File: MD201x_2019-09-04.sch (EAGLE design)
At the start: 103 parts, among them IC1 78L05F, IC2 LM321MF, J1 8P8C-LED, J10 1744446-4, J2 1744446-4, J3 XH-4-SIDE, J4 MA04-2, J5 MA05-2, J6 MA02-2, Q1 N-MOSFET-, Q2 N-MOSFET-, Q3 N-MOSFET-, Q4 N-MOSFET-, Q5 BSS123, U1 STM32F103C8, U10 XC6206, U2 NCV7351D1E, U3 SI8621AB-B-IS, U4 TLP184, U5 NCP5106D, U6 NCP5106D, U7 NCS199, U8 7815DT, U9 7805DT, X1 CSTCE8M00G55

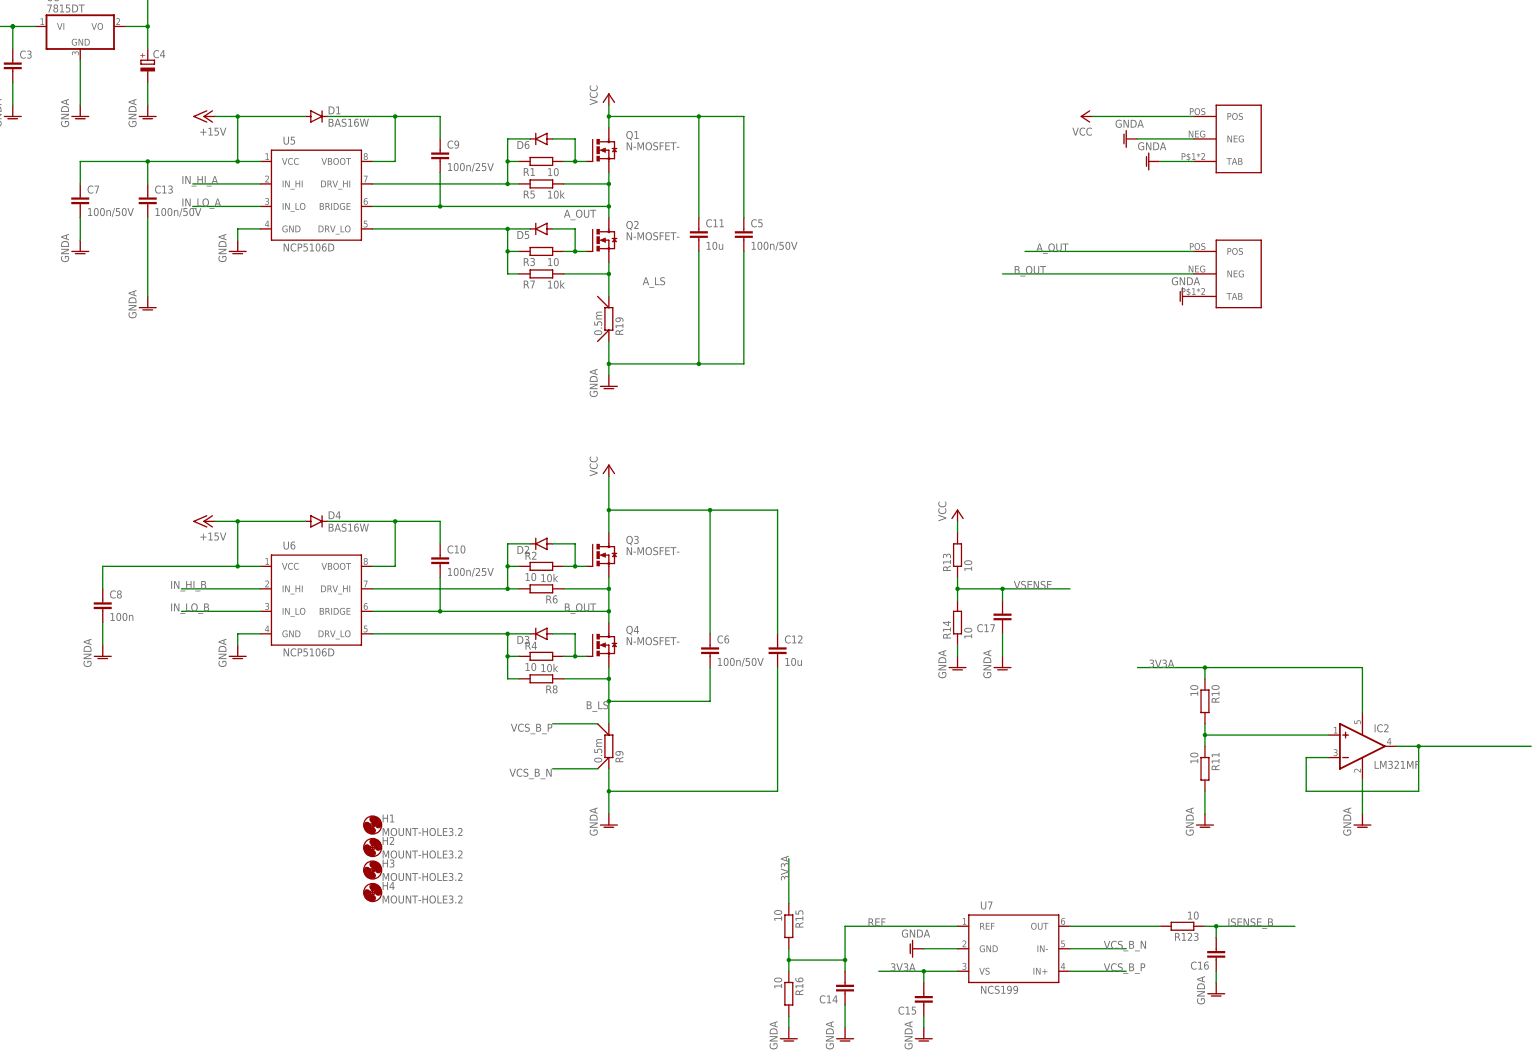
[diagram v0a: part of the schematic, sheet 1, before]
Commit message: エンコーダとand回路周りの修正
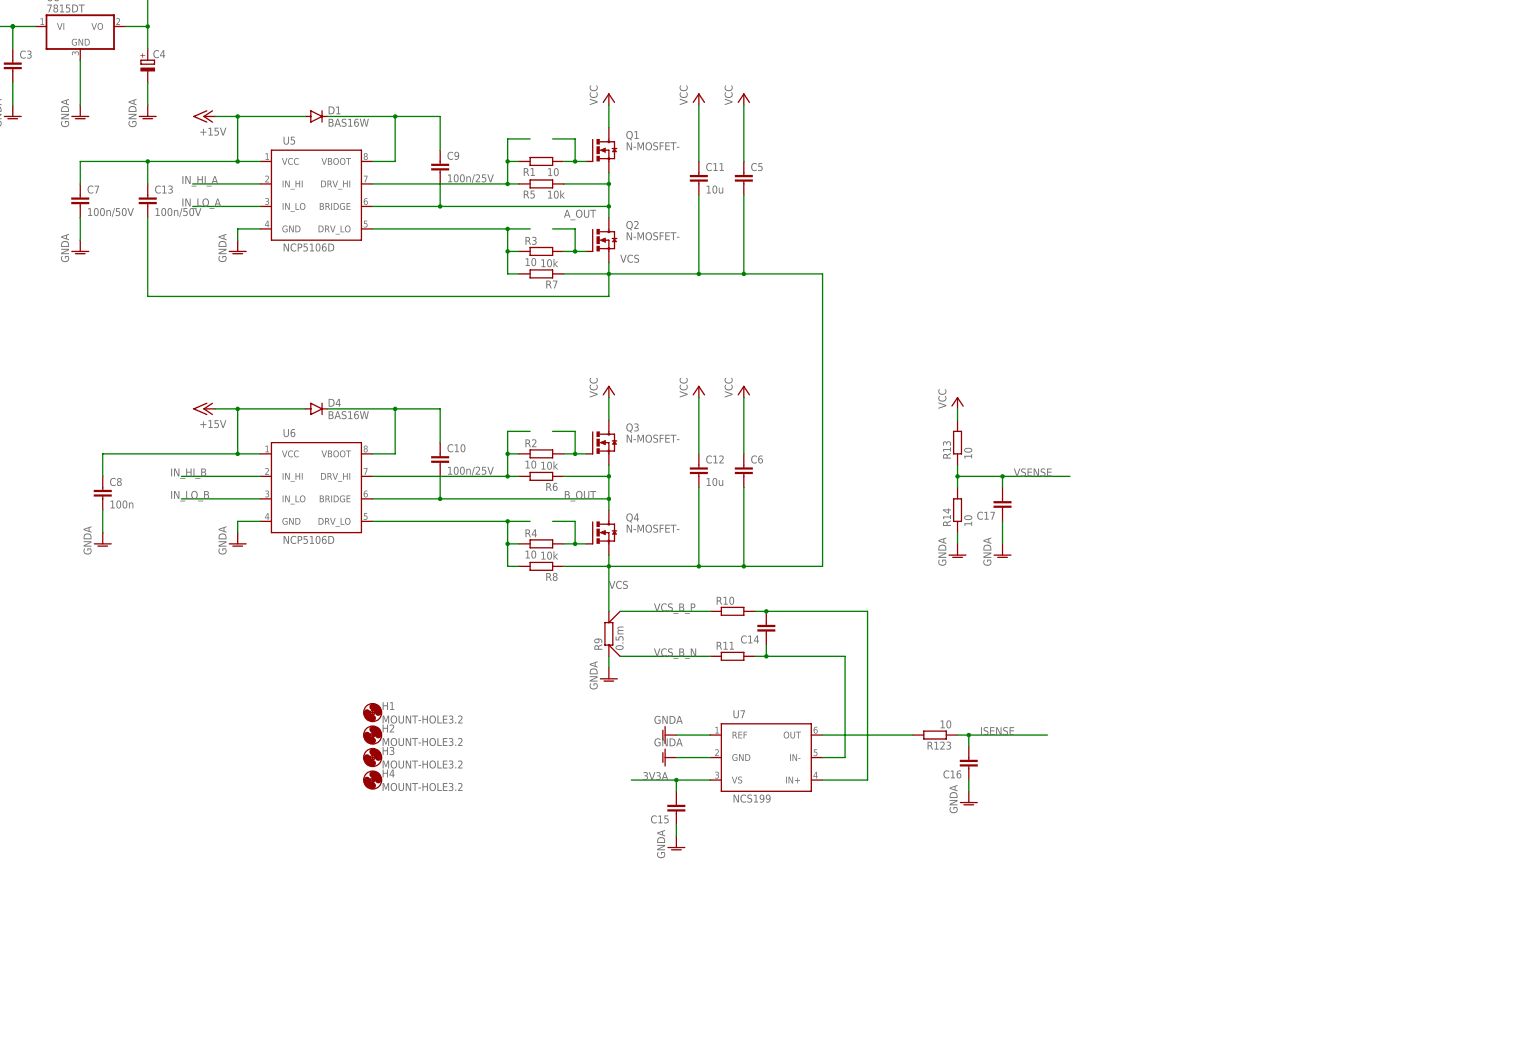
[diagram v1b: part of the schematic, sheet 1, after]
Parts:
- removed CN1: (no value), jst-xa:S4B-XASK-1
- removed D2, D3, D5, D6: (no value), diode:DIODE-SOD523
- removed IC1: 78L05F, linear:78L05F
- removed IC2: LM321MF, linear:LM321MF
- removed J10: 1744446-4, con-ep25:1744446-4
- removed J3: XH-4-SIDE, con-xh:XH-4-SIDE
- removed Q5: BSS123, transistor-small-signal:BSS123
- removed U$2: XT60PW-F, lib_ysk:XT60PW-F
- added C31: 22u, rcl:CPOL-EUE2.5-5
- added C32: 100n, rcl:C-EUC0603
- added C35: 220p, rcl:C-EUC0603
- added F1: (no value), rcl:R-EU_R1206
- added R22, R23: 100k, rcl:R-EU_R0603
- added R24: 100R, rcl:R-EU_R0603
- added U11: 7805DT, linear:7805DT
- added U12, U13, U14, U15: 74AHC1G08DCK, 74xx-little-us:74AHC1G08DCK
- C33: device rcl:C-EUC0603 -> rcl:C-EUC0805
- C36: value 100n -> 220p; device rcl:C-EUC1210 -> rcl:C-EUC0603
- C5, C6: value 100n/50V -> (none)
- J2: value 1744446-4 -> 1744426-4; device con-ep25:1744446-4 -> EP2.5:1744426-4
- R10, R11: value 10 -> (none)
- R15, R16: value 10 -> 100R
- R17: value 1k -> 100R
- R18: value 47k -> 100k
- R19: value 0.5m -> 100k; device r_shunt:CSS2H-2512 -> rcl:R-EU_R0603
- U$1: value XT60PW-M -> XH-4-SIDE; device lib_ysk:XT60PW-M -> con-xh:XH-4-SIDE
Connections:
- net CANRX_ISO renamed N$27
- net CANTX_ISO renamed N$23
- removed net A_LS: Q2.SOURCE, R19.2, R7.1
- removed net B_LS: C6.2, Q4.SOURCE, R8.1, R9.2
- removed net DC_ISO: C36.1, IC1.VI, J1.4, J1.5, R20.1
- removed net ISENSE_B: C16.2, R123.1
- removed net N$14: IC2.+IN, R10.2, R11.1
- removed net N$24: IC2.-IN, IC2.OUT
- removed net REF: C14.2, R15.2, R16.1, U7.REF
- new net 24V_ISO: C31.+, C32.1, F1.1, U11.VI
- new net N$15: R17.2, U$1.4
- new net N$30: R28.1, U4.AC1
- new net N$36: C14.2, R10.2, U7.IN+
- new net N$37: C14.1, R11.2, U7.IN-
- new net VCS: C11.2, C12.2, C13.2, C5.2, C6.2, Q2.SOURCE, Q4.SOURCE, R7.1, R8.1, R9.2
- net !EMS: now also U12A.I0, U13A.I0, U14A.I0, U15A.I0
- net !EMS_ISO: no longer R18.2
- net +3V3: now also U$1.2, U12P.VCC, U13P.VCC, U14P.VCC, U15P.VCC
- net +5V: now also J2.2; no longer J10P2.1, J3.2
- net 3V3A: no longer IC2.V+, R10.1, R15.1
- net 5V_ISO: now also U11.VO; no longer IC1.VO, R17.2
- net A_OUT: no longer U$2.POS
- net B_OUT: no longer U$2.NEG
- net CANH: now also J6.1
- net CANL: now also R12.1
- net ENC_A: now also C36.2, R15.1, U1.PA0-WKUP; no longer J10P3.1, U1.PB6
- net ENC_B: now also C35.2, R16.1, U1.PA1; no longer J10P4.1, U1.PB7
- net GNDA: now also C35.1, C36.1, J2.1, R18.2, R19.2, R22.2, R23.2, U$1.1, U12P.GND, U13P.GND, U14P.GND, U15P.GND, U7.REF; no longer C11.2, C12.2, C13.2, C14.1, C5.2, IC2.V-, J10P1.1, J3.1, R11.2, R16.2, R19.1, U$1.NEG, U$1.TAB, U$2.TAB
- net GNDIO: now also C31.-, C32.2, U11.GND, U4.AC2; no longer C36.2, IC1.GND, IC1.GND@1, Q5.S, R18.1
- net IN_A: now also R24.1; no longer J3.3
- net IN_B: now also R17.1; no longer J3.4
- net IN_HI_A: now also U13A.O
- net IN_HI_A_PRE: now also R18.1, U13A.I1
- net IN_HI_B: now also U14A.O
- net IN_HI_B_PRE: now also R19.1, U14A.I1
- net IN_LO_A: now also U12A.O
- net IN_LO_A_PRE: now also R22.1, U12A.I1
- net IN_LO_B: now also U15A.O
- net IN_LO_B_PRE: now also R23.1, U15A.I1
- net ISENSE: now also C16.2, R123.1
- net N$1: no longer D6.C
- net N$11: no longer D5.C
- net N$12: now also J2.4, R16.2; no longer D2.A, Q3.GATE, R2.2
- net N$13: now also Q3.GATE, R2.2; no longer J6.1
- net N$16: now also J2.3, R15.2; no longer R17.1, U4.AC1
- net N$17: now also R24.2, U$1.3; no longer Q5.D, U4.AC2
- net N$2: no longer D2.C
- net N$4: no longer D6.A
- net N$5: no longer D3.C
- net N$61: no longer D5.A
- net N$64: no longer D3.A
- net N$8: now also F1.2, J1.4, J1.5, R20.1; no longer Q5.G, R28.1
- net UART_RX: now also U1.PB7
- net UART_TX: now also U1.PB6
- net VCC: no longer U$1.POS
- net VCS_B_N: now also R11.1; no longer U7.IN-
- net VCS_B_P: now also R10.1; no longer U7.IN+
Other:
- note removed: "TODO: BOOT0をジャンパで切り替えられるようにする"
- note removed: "TODO: PWM信号を直列終端する"
- note removed: "TODO: エンコーダ入力を5Vトレラントにする"
- note removed: "TODO: デバッガ用コネクタを最適化する"
- moved on the sheet: C10, C11, C12, C14, C15, C16, C17, C5, C6, C8, C9, D4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
